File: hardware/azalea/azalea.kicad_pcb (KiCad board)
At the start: 4 copper layers, 70.7 x 53.3 mm, 88 parts, among them J1 NEIGHBOR1, J2 NEIGHBOR2, J3 USB-MICRO-B-SHIELDED, J4 USB-MICRO-B-SHIELDED, J5 JTAG, J7 BONUS_ROW, SW1 DFU, SW2 RESET, U1 LPC4330FBD144, U2 W25Q16DV, U3 AP7333, U4 IP4220CZ6, U5 NX5P2553GV, X1 XTAL4PIN, X2 RTC_XTAL

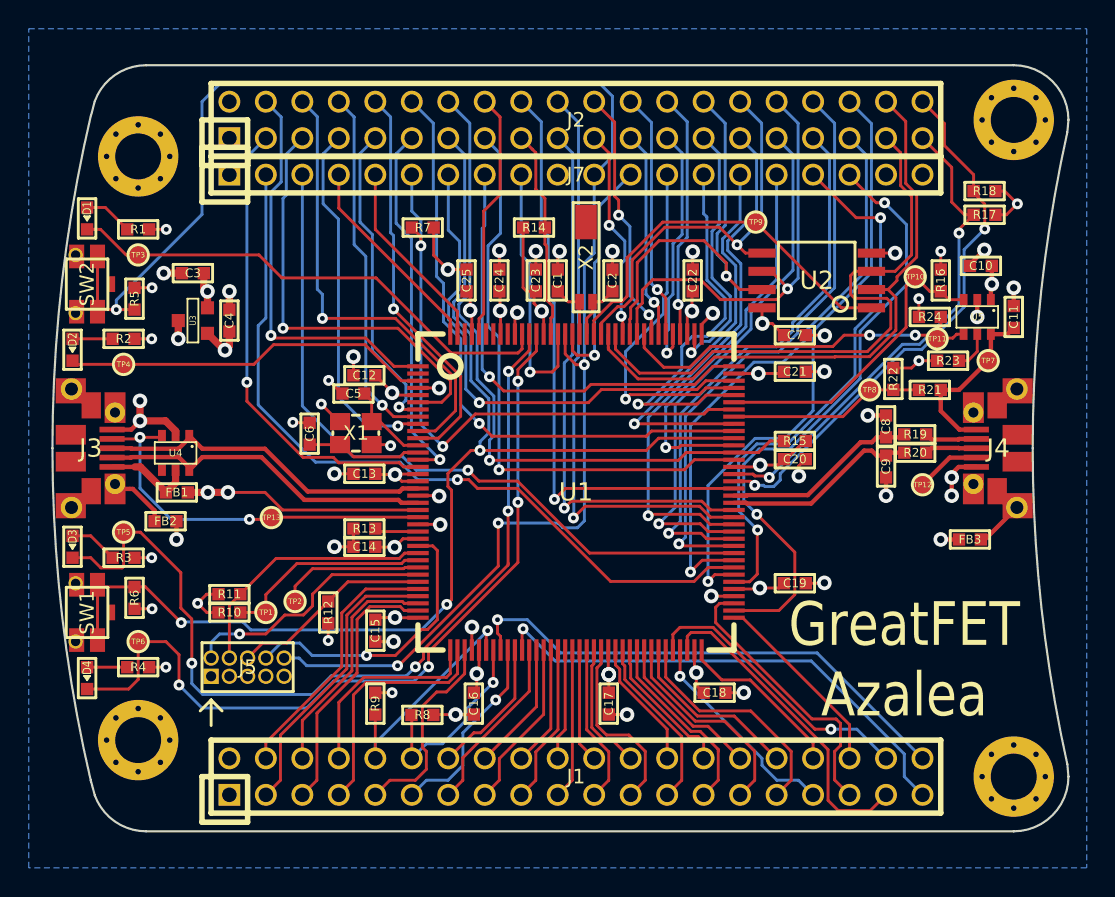
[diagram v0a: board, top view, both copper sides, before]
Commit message: azalea: corrected DRC errors
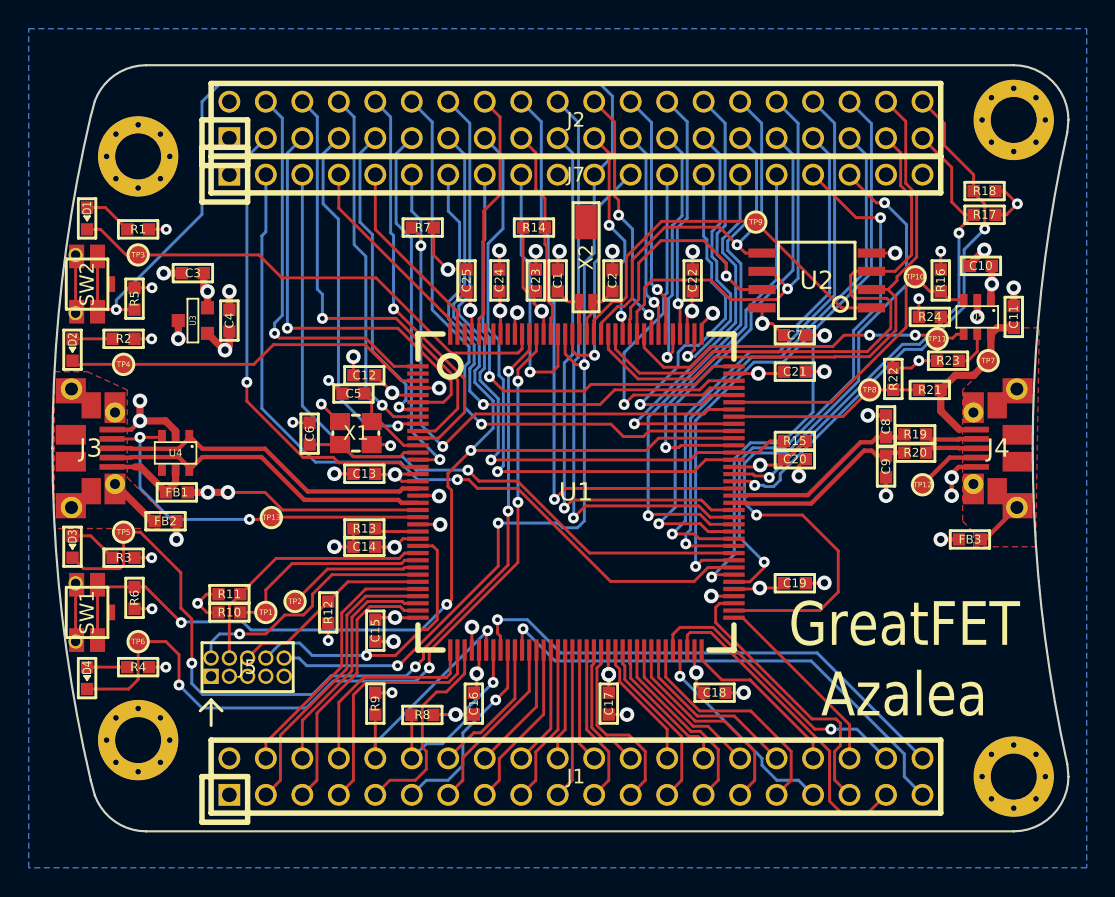
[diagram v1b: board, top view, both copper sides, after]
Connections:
- net Net-(FB2-Pad2) renamed /USB0_SHIELD
- net Net-(FB3-Pad1) renamed /USB1_SHIELD
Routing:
- net /P6_1: track 43.4 -> 49.4 mm
- net GND: track 75.5 -> 79.6 mm
- net VCC: track 76.9 -> 81.0 mm
- net /P2_1: track 40.3 -> 39.3 mm
- net /P7_0: track 18.9 -> 19.7 mm
- net /P2_8: track 84.3 -> 85.1 mm
- net /P6_3: track 42.0 -> 41.3 mm
- net /P2_6: track 40.9 -> 41.6 mm
- net /P2_11: track 24.7 -> 25.4 mm
- net /P6_6: track 41.0 -> 40.3 mm
- net /TRST: track 10.2 -> 9.54 mm
- net /P7_1: track 17.3 -> 17.9 mm
- net /P2_10: track 27.0 -> 26.4 mm
- added copper zone on F.Cu, net /USB0_SHIELD
- added copper zone on F.Cu, net /USB1_SHIELD

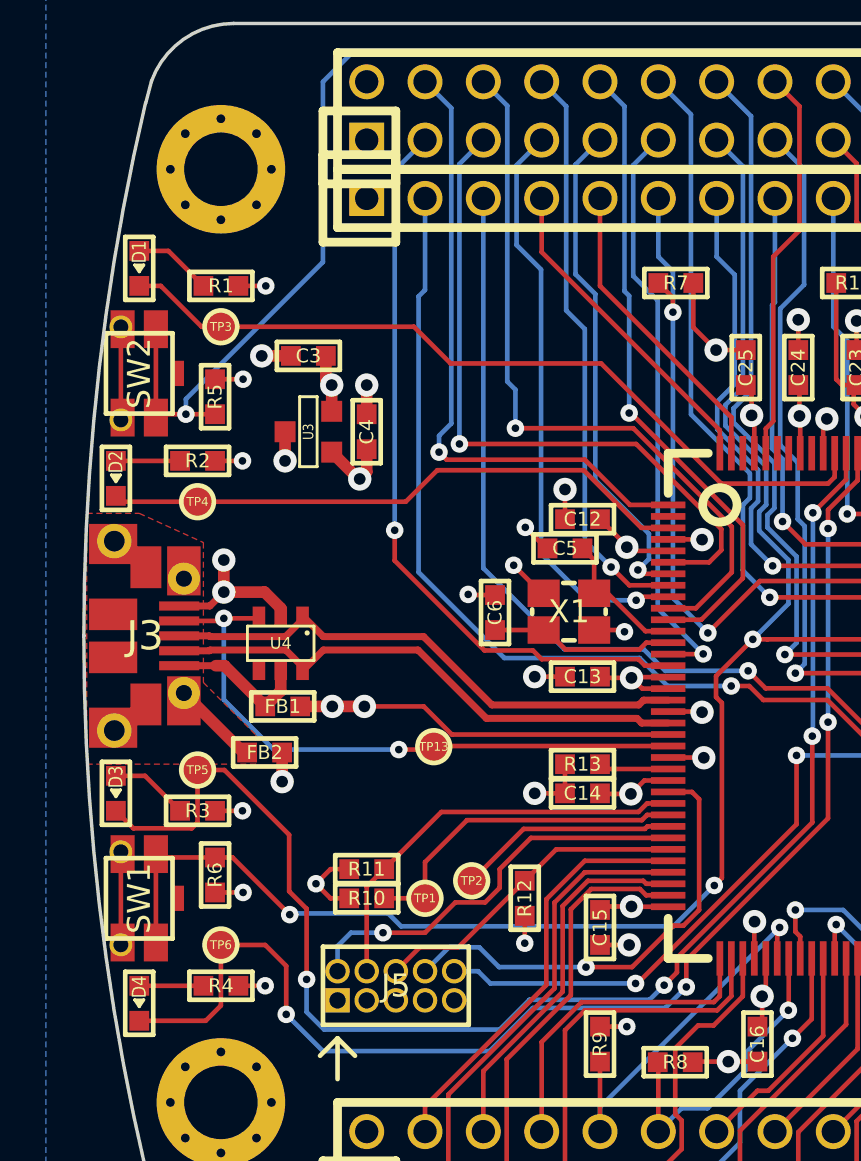
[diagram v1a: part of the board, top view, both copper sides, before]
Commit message: azalea: power supply zones
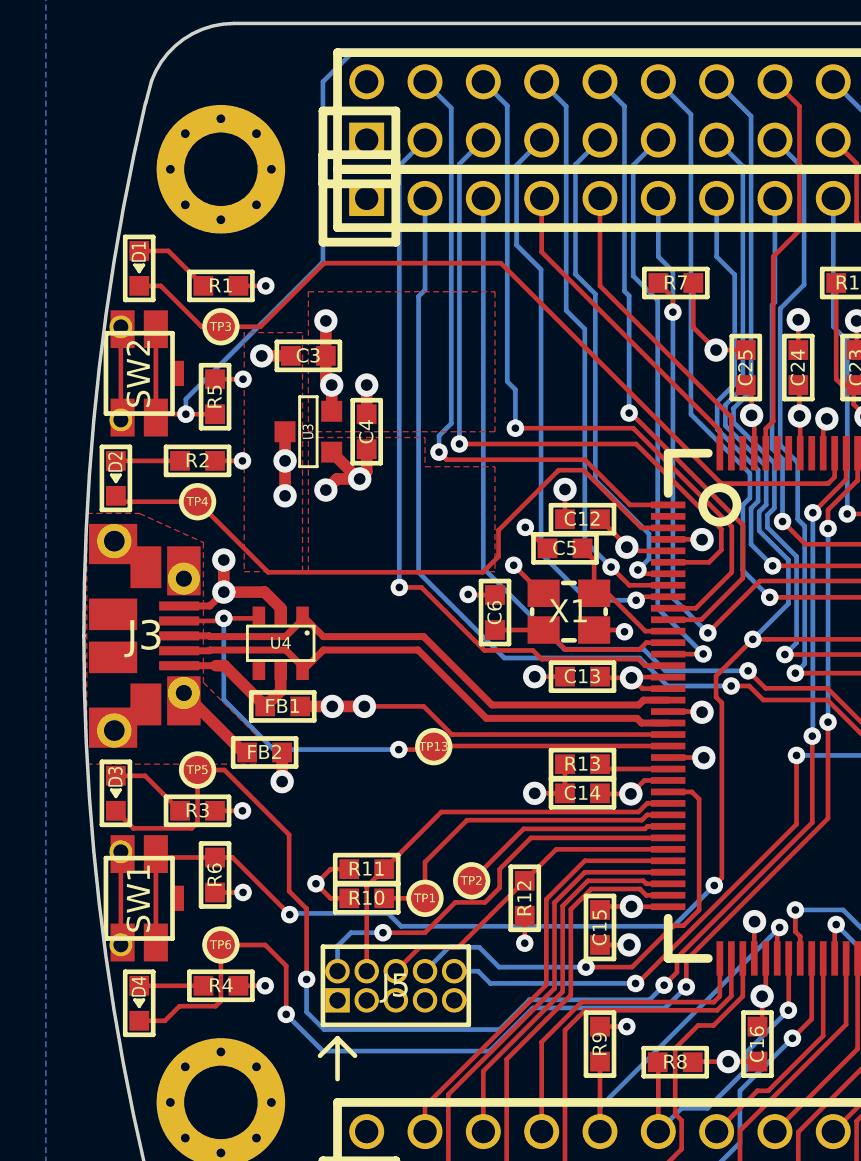
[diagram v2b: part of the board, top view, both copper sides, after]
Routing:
- net /LED2: track 25.8 -> 29.0 mm
- net /LED1: track 35.2 -> 37.3 mm
- net /VBUS: track 22.0 -> 23.7 mm, vias 4 -> 5
- net GND: track 79.6 -> 81.1 mm, vias 46 -> 47
- net VCC: track 81.0 -> 82.5 mm, vias 27 -> 28
- added copper zone on F.Cu, net /VBUS
- added copper zone on F.Cu, net GND
- added copper zone on F.Cu, net VCC

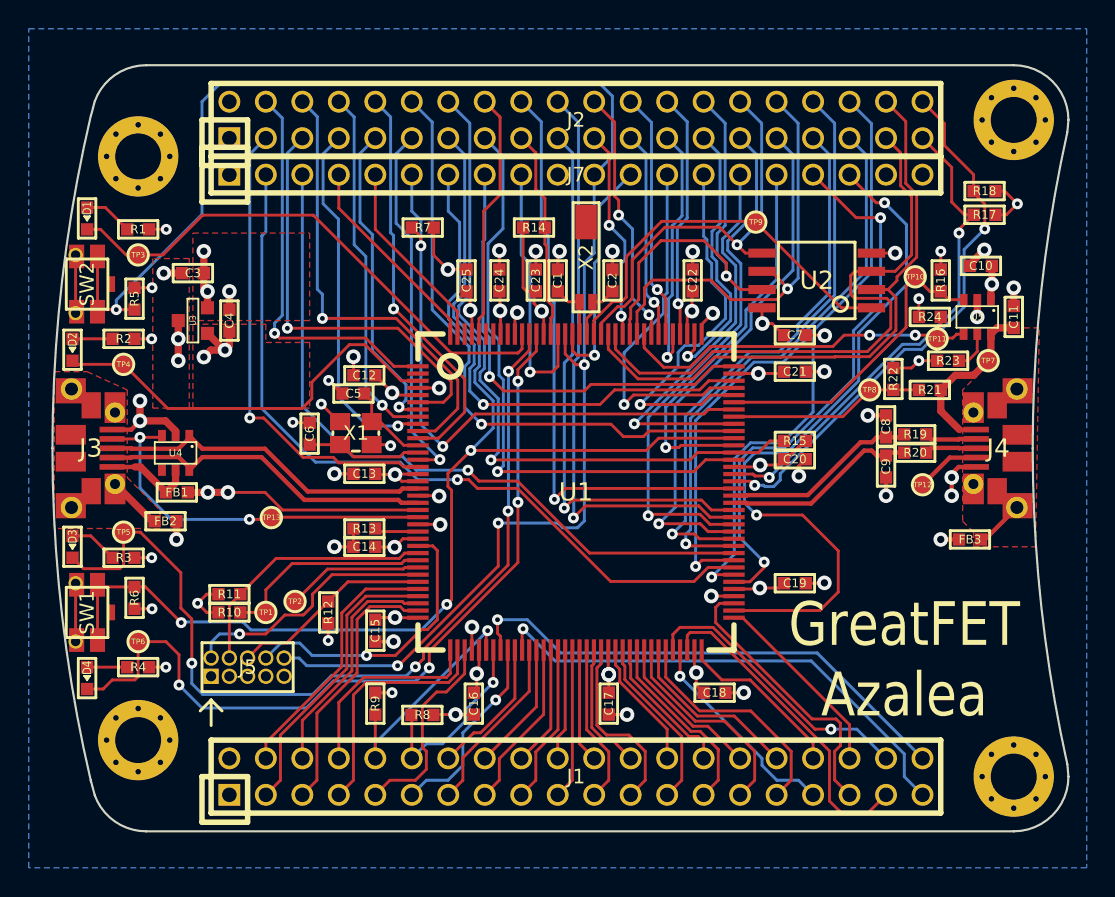
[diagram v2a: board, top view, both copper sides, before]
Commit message: azalea: edge cutouts for USB connectors, made PCB edge continuous
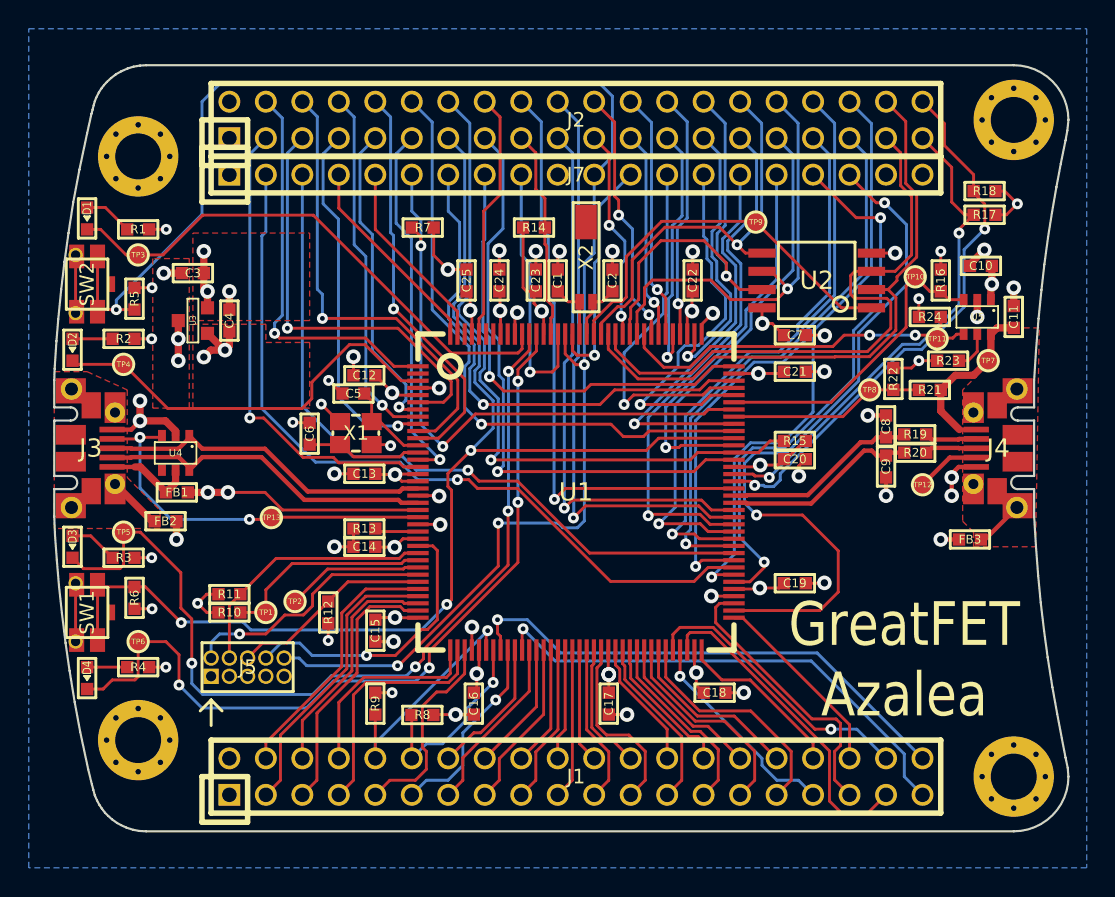
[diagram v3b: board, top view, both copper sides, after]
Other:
- board size 70.7 x 53.3 mm -> 70.6 x 53.3 mm

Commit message: azalea: silkscreen labels
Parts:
- moved TP3 4.32 mm to (115.6, 82.3)
- moved R6 1.78 mm to (113.3, 108.2)
- moved R5 1.61 mm to (113.0, 87.9)
- turned D1 to 81 degrees
- turned D2 to 86.1 degrees
- turned D3 to 93.9 degrees
- turned D4 to 99 degrees
- turned SW1 to 276.4 degrees
- turned SW2 to 263.6 degrees
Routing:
- net VCC: track 82.5 -> 84.9 mm, vias 28 -> 27
- net /RESET: track 113.6 -> 115.2 mm
- net /P2_8: track 85.1 -> 86.3 mm
- net /LED1: track 37.3 -> 36.7 mm
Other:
- board text added: "24 September 2015"
- board text added: "BONUS ROW!"
- board text added: "DFU"
- board text added: "GND"
- board text added: "I2C:"
- board text added: "J1"
- board text added: "J2"
- board text added: "J3"
- board text added: "J4"
- board text added: "J5"
- board text added: "J7"
- board text added: "LED1"
- board text added: "LED2"
- board text added: "LED3"
- board text added: "LED4"
- board text added: "MISO"
- board text added: "MOSI"
- board text added: "RESET"
- board text added: "SCK"
- board text added: "SCL"
- board text added: "SDA"
- board text added: "SPI:"
- board text added: "SSEL"
- board text added: "USB0 HOST"
- board text added: "USB1 TARGET"
- board text added: "VBUS"
- board text added: "VCC"
- board text added: "http://greatscottgadgets.com/"

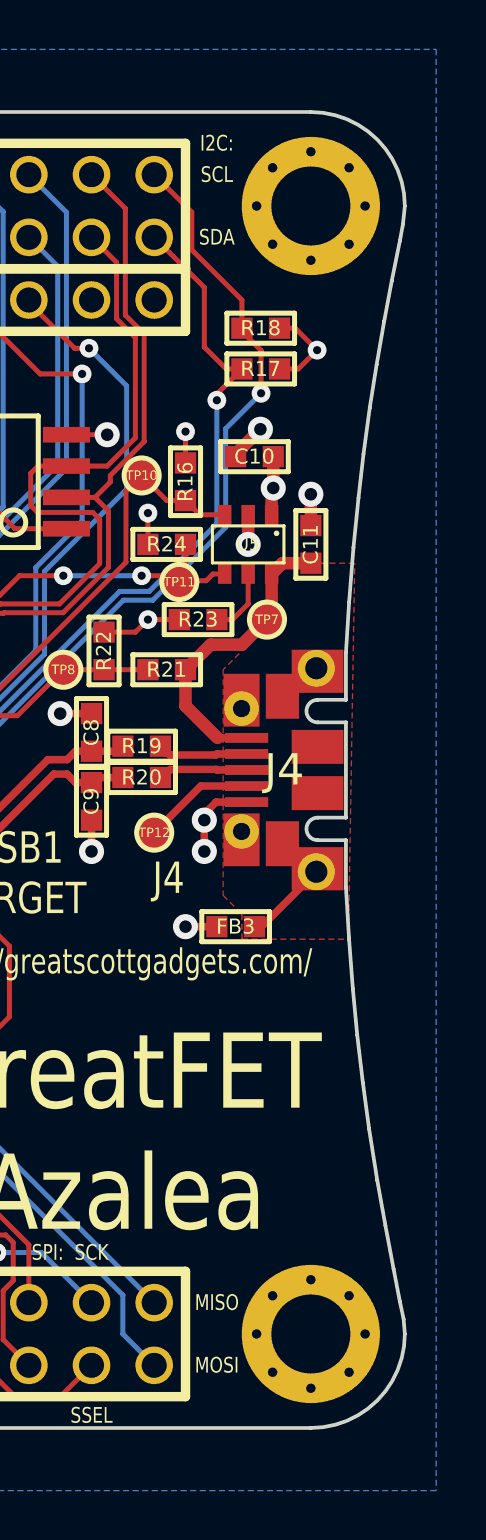
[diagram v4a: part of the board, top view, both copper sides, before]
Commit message: azalea: added layer legend, renamed inner layers
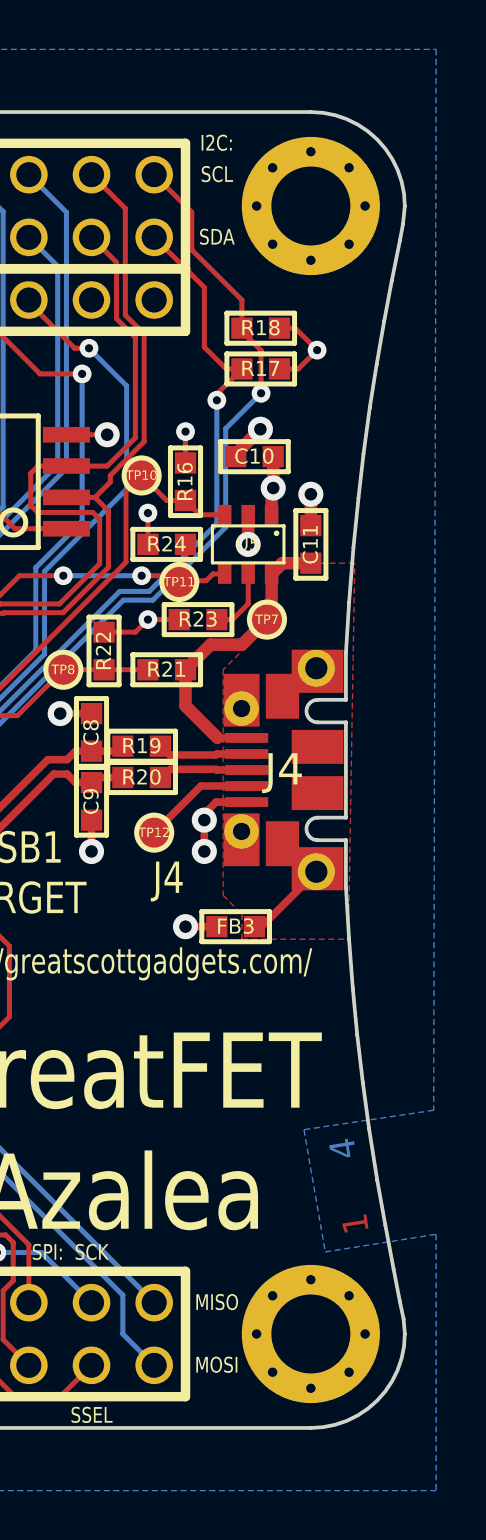
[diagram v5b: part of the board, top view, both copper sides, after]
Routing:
- added copper zone on C2.Cu, net GND
- added copper zone on C3.Cu, net VCC
- removed copper zone on In1.Cu, net GND
- removed copper zone on In2.Cu, net VCC
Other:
- board text added: "1"
- board text added: "2"
- board text added: "3"
- board text added: "4"
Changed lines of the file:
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@@
     (area 93.271704 68.58 275.715801 199.465001)
     (thickness 1.6)
-    (drawings 142)
+    (drawings 146)
     (tracks 1433)
     (zones 0)
@@
   (layers
     (0 F.Cu signal)
-    (1 In1.Cu signal)
-    (2 In2.Cu signal)
+    (1 C2.Cu power)
+    (2 C3.Cu power)
     (31 B.Cu signal)
     (33 F.Adhes user)
@@
     (39 F.Mask user)
     (40 Dwgs.User user)
-    (41 Cmts.User user hide)
+    (41 Cmts.User user)
     (42 Eco1.User user)
     (43 Eco2.User user)
@@
     (pcbplotparams
       (layerselection 0x010a8_80000007)
-      (usegerberextensions false)
+      (usegerberextensions true)
       (excludeedgelayer true)
       (linewidth 0.100000)
@@
       (psnegative false)
       (psa4output false)
-      (plotreference true)
-      (plotvalue true)
+      (plotreference false)
+      (plotvalue false)
       (plotinvisibletext false)
       (padsonsilk false)
@@
       (drillshape 0)
       (scaleselection 1)
-      (outputdirectory ""))
+      (outputdirectory gerber))
   )
   (net 0 "")
@@
       (net 16 /LED4) (die_length 0.08382) (solder_mask_margin 0.1016) (clearance 0.1778))
   )
+  (gr_text 4 (at 174.0408 113.1316 98.9) (layer B.Cu)
+    (effects (font (size 1.016 1.016) (thickness 0.1778)))
+  )
+  (gr_text 3 (at 174.2186 114.173 98.9) (layer C3.Cu)
+    (effects (font (size 1.016 1.016) (thickness 0.1778)))
+  )
+  (gr_text 2 (at 174.371 115.1636 98.9) (layer C2.Cu)
+    (effects (font (size 1.016 1.016) (thickness 0.1778)))
+  )
+  (gr_text 1 (at 174.5488 116.1796 98.9) (layer F.Cu)
+    (effects (font (size 1.016 1.016) (thickness 0.1778)))
+  )
   (gr_line (start 128.8034 81.026) (end 129.2098 81.6102) (angle 90) (layer F.SilkS) (width 0.2032))
   (gr_line (start 128.27 81.534) (end 128.778 81.026) (angle 90) (layer F.SilkS) (width 0.2032))
@@
   (segment (start 172.9424 101.915) (end 170.7174 104.14) (width 0.3048) (layer F.Cu) (net 138) (status 30))
   (segment (start 170.7174 104.14) (end 170.434 104.14) (width 0.3048) (layer F.Cu) (net 138) (status 30))
-  (zone (net 1) (net_name GND) (layer In1.Cu) (hatch edge 0.508)
+  (zone (net 1) (net_name GND) (layer C2.Cu) (hatch edge 0.508)
     (connect_pads (clearance 0.254))
     (min_thickness 0.254)
@@
     (polygon
       (pts
-        (xy 104.14 68.58) (xy 177.8 68.58) (xy 177.8 127) (xy 104.14 127)
+        (xy 104.14 68.58) (xy 177.8 68.58) (xy 177.6984 111.5822) (xy 172.4406 112.3696) (xy 173.3042 117.3226)
+        (xy 177.8254 116.6114) (xy 177.8 127) (xy 104.14 127)
       )
     )
   )
-  (zone (net 4) (net_name VCC) (layer In2.Cu) (hatch edge 0.508)
+  (zone (net 4) (net_name VCC) (layer C3.Cu) (hatch edge 0.508)
     (connect_pads (clearance 0.254))
     (min_thickness 0.254)
@@
     (polygon
       (pts
-        (xy 104.14 68.58) (xy 177.8 68.58) (xy 177.8 127) (xy 104.14 127)
+        (xy 104.14 68.58) (xy 177.8 68.58) (xy 177.6984 111.5822) (xy 172.4406 112.3696) (xy 173.3042 117.3226)
+        (xy 177.8 116.6114) (xy 177.8 127) (xy 104.14 127)
       )
     )
@@
     (polygon
       (pts
-        (xy 104.14 68.58) (xy 177.8 68.58) (xy 177.8 127) (xy 104.14 127)
+        (xy 104.14 68.58) (xy 177.8 68.58) (xy 177.6984 111.5822) (xy 172.4406 112.3696) (xy 173.3042 117.3226)
+        (xy 177.8 116.6114) (xy 177.8 127) (xy 104.14 127)
       )
     )
